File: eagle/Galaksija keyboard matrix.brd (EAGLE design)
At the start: 223.5 x 94 mm, 58 parts

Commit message: New version Rev.2
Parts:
- removed JP1: to LS251, pinhead:1X08
- removed JP2: to LS145, pinhead:1X08
- added LED1: PWR, led:LED5MM
- added R1: 1k, rcl:0207/10
- added S57: RST, switch-omron:B3F-40XX
- added SV1: KBD, con-harting-ml:ML20
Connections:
- removed net IN0: JP1.8, S17.3, S17.4, S25.3, S25.4, S33.3, S33.4, S41.3, S41.4, S49.3, S49.4, S9.3, S9.4
- removed net IN1: JP1.7, S10.3, S10.4, S18.3, S18.4, S2.3, S2.4, S26.3, S26.4, S34.3, S34.4, S42.3, S42.4, S50.3, S50.4
- removed net IN2: JP1.6, S11.3, S11.4, S19.3, S19.4, S27.3, S27.4, S3.3, S3.4, S35.3, S35.4, S43.3, S43.4, S51.3, S51.4
- removed net IN3: JP1.5, S12.3, S12.4, S20.3, S20.4, S28.3, S28.4, S36.3, S36.4, S4.3, S4.4, S44.3, S44.4, S52.3, S52.4
- removed net IN4: JP1.4, S13.3, S13.4, S21.3, S21.4, S29.3, S29.4, S37.3, S37.4, S45.3, S45.4, S5.3, S5.4, S53.3, S53.4
- removed net IN5: JP1.3, S14.3, S14.4, S22.3, S22.4, S30.3, S30.4, S38.3, S38.4, S46.3, S46.4, S54.3, S54.4, S55.3, S55.4, S6.3, S6.4
- removed net IN6: JP1.2, S15.3, S15.4, S23.3, S23.4, S31.3, S31.4, S39.3, S39.4, S47.3, S47.4, S7.3, S7.4
- removed net IN7: JP1.1, S1.3, S1.4, S16.3, S16.4, S24.3, S24.4, S32.3, S32.4, S40.3, S40.4, S48.3, S48.4, S56.3, S56.4, S8.3, S8.4
- new net D7: S1.3, S1.4, S16.3, S16.4, S24.3, S24.4, S32.3, S32.4, S40.3, S40.4, S48.3, S48.4, S56.3, S56.4, S8.3, S8.4, SV1.4
- new net GND: LED1.K, SV1.2, SV1.20
- new net N$1: LED1.A, R1.2
- new net Q0: S2.1, S2.2, S3.1, S3.2, S4.1, S4.2, S5.1, S5.2, S6.1, S6.2, S7.1, S7.2, S8.1, S8.2, SV1.3
- new net Q1: S10.1, S10.2, S11.1, S11.2, S12.1, S12.2, S13.1, S13.2, S14.1, S14.2, S15.1, S15.2, S16.1, S16.2, S9.1, S9.2, SV1.5
- new net Q2: S17.1, S17.2, S18.1, S18.2, S19.1, S19.2, S20.1, S20.2, S21.1, S21.2, S22.1, S22.2, S23.1, S23.2, S24.1, S24.2, SV1.7
- new net Q3: S1.1, S1.2, S25.1, S25.2, S26.1, S26.2, S27.1, S27.2, S28.1, S28.2, S29.1, S29.2, S30.1, S30.2, S31.1, S31.2, S32.1, S32.2, S56.1, S56.2, SV1.9
- new net Q4: S33.1, S33.2, S34.1, S34.2, S35.1, S35.2, S36.1, S36.2, S37.1, S37.2, S38.1, S38.2, S39.1, S39.2, S40.1, S40.2, SV1.11
- new net Q5: S41.1, S41.2, S42.1, S42.2, S43.1, S43.2, S44.1, S44.2, S45.1, S45.2, S46.1, S46.2, S47.1, S47.2, S48.1, S48.2, SV1.13
- new net Q6: S49.1, S49.2, S50.1, S50.2, S51.1, S51.2, S52.1, S52.2, S53.1, S53.2, S54.1, S54.2, S55.1, S55.2, SV1.15
- new net RST: S57.1, S57.2, SV1.19
- new net VCC: R1.1, S57.3, S57.4, SV1.1
- net D0: now also S17.3, S17.4, S25.3, S25.4, S33.3, S33.4, S41.3, S41.4, S49.3, S49.4, S9.3, S9.4, SV1.18; no longer JP2.1, S2.1, S2.2, S3.1, S3.2, S4.1, S4.2, S5.1, S5.2, S6.1, S6.2, S7.1, S7.2, S8.1, S8.2
- net D1: now also S10.3, S10.4, S18.3, S18.4, S2.3, S2.4, S26.3, S26.4, S34.3, S34.4, S42.3, S42.4, S50.3, S50.4, SV1.16; no longer JP2.2, S10.1, S10.2, S11.1, S11.2, S12.1, S12.2, S13.1, S13.2, S14.1, S14.2, S15.1, S15.2, S16.1, S16.2, S9.1, S9.2
- net D2: now also S11.3, S11.4, S19.3, S19.4, S27.3, S27.4, S3.3, S3.4, S35.3, S35.4, S43.3, S43.4, S51.3, S51.4, SV1.14; no longer JP2.3, S17.1, S17.2, S18.1, S18.2, S19.1, S19.2, S20.1, S20.2, S21.1, S21.2, S22.1, S22.2, S23.1, S23.2, S24.1, S24.2
- net D3: now also S12.3, S12.4, S20.3, S20.4, S28.3, S28.4, S36.3, S36.4, S4.3, S4.4, S44.3, S44.4, S52.3, S52.4, SV1.12; no longer JP2.4, S1.1, S1.2, S25.1, S25.2, S26.1, S26.2, S27.1, S27.2, S28.1, S28.2, S29.1, S29.2, S30.1, S30.2, S31.1, S31.2, S32.1, S32.2, S56.1, S56.2
- net D4: now also S13.3, S13.4, S21.3, S21.4, S29.3, S29.4, S37.3, S37.4, S45.3, S45.4, S5.3, S5.4, S53.3, S53.4, SV1.10; no longer JP2.5, S33.1, S33.2, S34.1, S34.2, S35.1, S35.2, S36.1, S36.2, S37.1, S37.2, S38.1, S38.2, S39.1, S39.2, S40.1, S40.2
- net D5: now also S14.3, S14.4, S22.3, S22.4, S30.3, S30.4, S38.3, S38.4, S46.3, S46.4, S54.3, S54.4, S55.3, S55.4, S6.3, S6.4, SV1.8; no longer JP2.6, S41.1, S41.2, S42.1, S42.2, S43.1, S43.2, S44.1, S44.2, S45.1, S45.2, S46.1, S46.2, S47.1, S47.2, S48.1, S48.2
- net D6: now also S15.3, S15.4, S23.3, S23.4, S31.3, S31.4, S39.3, S39.4, S47.3, S47.4, S7.3, S7.4, SV1.6; no longer JP2.7, S49.1, S49.2, S50.1, S50.2, S51.1, S51.2, S52.1, S52.2, S53.1, S53.2, S54.1, S54.2, S55.1, S55.2
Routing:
- net IN7: track 462.2 -> 0.00 mm, vias 1 -> 0
- net Q3: track 0.00 -> 450.8 mm, vias 0 -> 3
- net D7: track 0.00 -> 408.5 mm, vias 0 -> 1
- net IN4: track 406.6 -> 0.00 mm, vias 1 -> 0
- net IN5: track 397.8 -> 0.00 mm, vias 1 -> 0
- net IN3: track 397.7 -> 0.00 mm
- net Q5: track 0.00 -> 365.7 mm
- net IN6: track 354.9 -> 0.00 mm
- net Q4: track 0.00 -> 342.5 mm
- net IN2: track 339.7 -> 0.00 mm, vias 1 -> 0
- net IN1: track 337.3 -> 0.00 mm
- net Q2: track 0.00 -> 330.9 mm, vias 0 -> 3
- net Q6: track 0.00 -> 322.2 mm
- net VCC: track 0.00 -> 291.9 mm
- net IN0: track 277.4 -> 0.00 mm
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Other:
- board size 223.5 x 94 mm -> 233.7 x 99.1 mm
- board text added: "Galaksija 08/2022 keyboard matrix rev.2 by hans"
- board text added: "Q0"
- board text added: "Q1"
- board text added: "Q2"
- board text added: "Q3"
- board text added: "Q4"
- board text added: "Q5"
- board text added: "Q6"
- board text added: "Reset"
- board text removed: "Galaksija 08/2022 keyboard matrix rev.1 by hans"

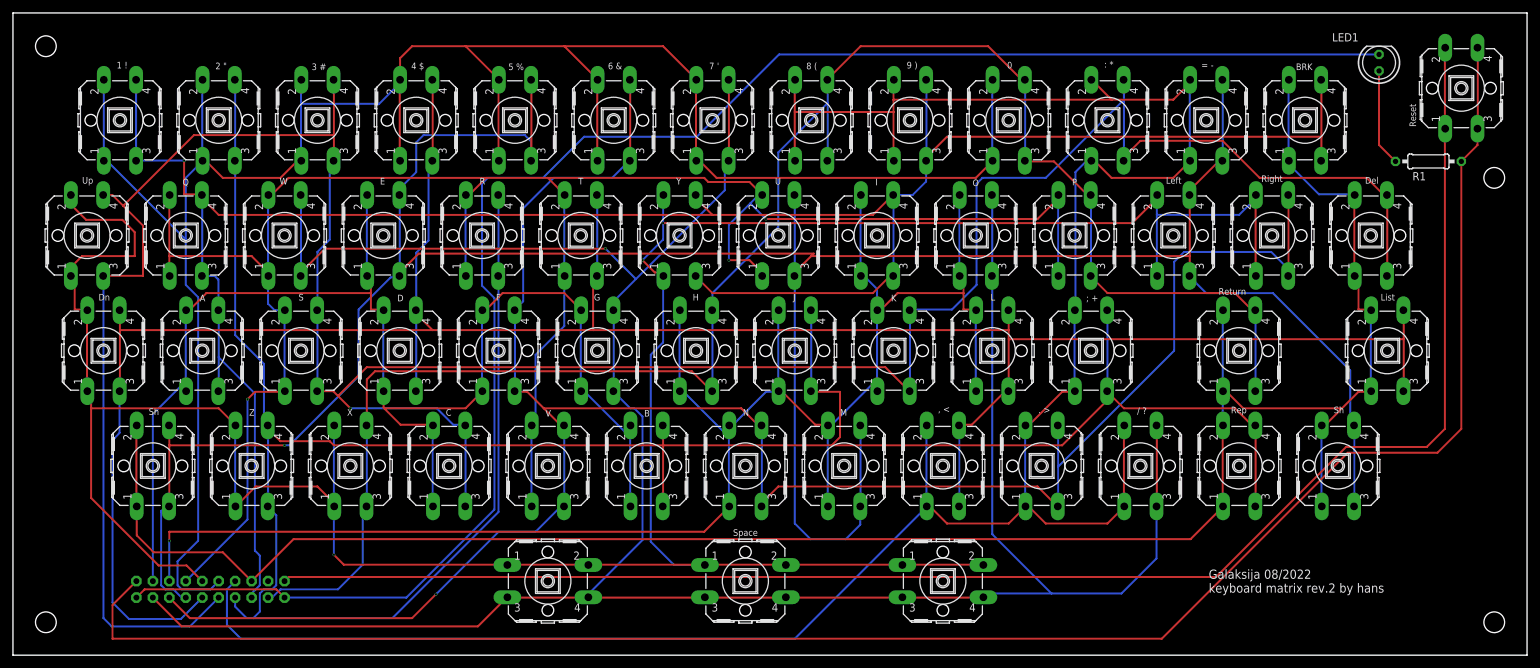
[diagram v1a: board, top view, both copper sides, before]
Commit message: Rev3 narrower version with modified ENTER key
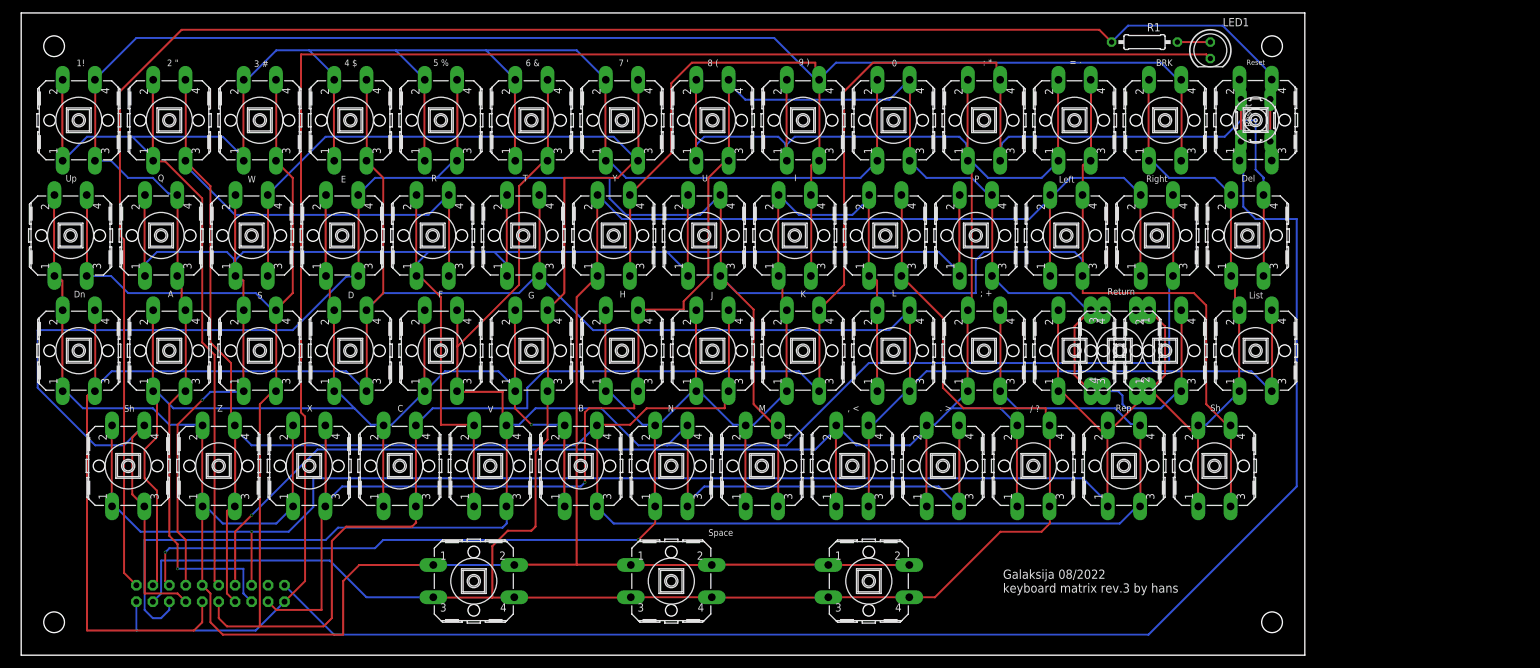
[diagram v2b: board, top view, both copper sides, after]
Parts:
- added S58, S59: Return, switch-omron:B3F-40XX
- added S60: RST2, switch-omron:B3F-10XX
- moved R1 47.5 mm to (174.6, 94.6), turned to 0 degrees
- moved S57 32.1 mm to (191.8, 82.6)
- moved LED1 26.1 mm to (184.8, 93.3), turned to 270 degrees
- moved S49 25.4 mm to (163.8, 47.0)
- moved S50 21.6 mm to (177.8, 82.5)
- moved S46 20.3 mm to (163.8, 82.5)
- moved S53 20.3 mm to (191.8, 47.0)
- moved S52 19.1 mm to (190.5, 64.8)
- moved S55 19.1 mm to (185.4, 29.2)
- moved S44 19.0 mm to (149.9, 82.5)
- moved S31 17.8 mm to (176.5, 64.8)
- moved S33 17.8 mm to (135.9, 82.5)
- moved S51 17.8 mm to (171.4, 29.2)
- moved S48 16.5 mm to (157.5, 29.2)
- moved S42 16.5 mm to (121.9, 82.5)
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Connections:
- net D0: now also S58.3, S58.4, S59.3, S59.4
- net Q6: now also S58.1, S58.2, S59.1, S59.2
- net RST: now also S60.1, S60.2
- net VCC: now also S60.3, S60.4
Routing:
- net Q3: track 450.8 -> 405.1 mm, vias 3 -> 0
- net D6: track 332.5 -> 373.0 mm, vias 1 -> 0
- net D3: track 449.3 -> 419.3 mm, vias 1 -> 0
- net Q5: track 365.7 -> 338.5 mm, vias 0 -> 1
- net D1: track 356.3 -> 381.1 mm
- net D2: track 411.0 -> 386.6 mm
- net Q6: track 322.2 -> 340.7 mm, vias 0 -> 1
- net D7: track 408.5 -> 390.6 mm, vias 1 -> 0
- net Q1: track 268.4 -> 250.9 mm, vias 1 -> 2
- net D5: track 430.6 -> 413.2 mm, vias 1 -> 0
- net D0: track 277.4 -> 293.6 mm, vias 0 -> 1
- net VCC: track 291.9 -> 277.4 mm
- net Q4: track 342.5 -> 329.5 mm
- net Q0: track 215.1 -> 204.5 mm, vias 0 -> 1
- net N$1: track 15.0 -> 5.08 mm
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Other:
- board size 233.7 x 99.1 mm -> 198.1 x 99.1 mm
- board text added: "1!"
- board text added: "Galaksija 08/2022 keyboard matrix rev.3 by hans"
- board text removed: "1 !"
- board text removed: "Galaksija 08/2022 keyboard matrix rev.2 by hans"
